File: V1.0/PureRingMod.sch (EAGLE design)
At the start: 32 parts, among them IC1 TL074P, IC2 TL072P, X1 NC3FD-V

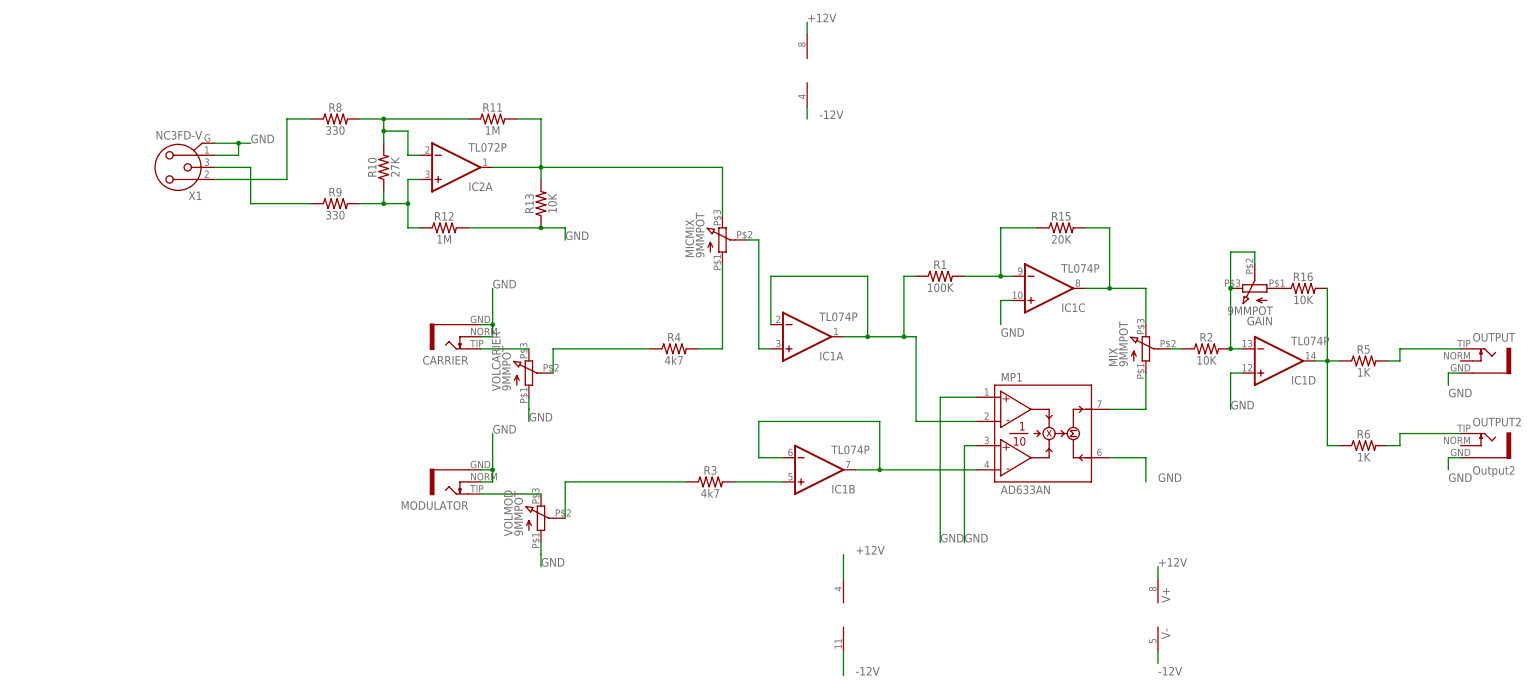
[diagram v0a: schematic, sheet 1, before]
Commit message: Panel layout and routing
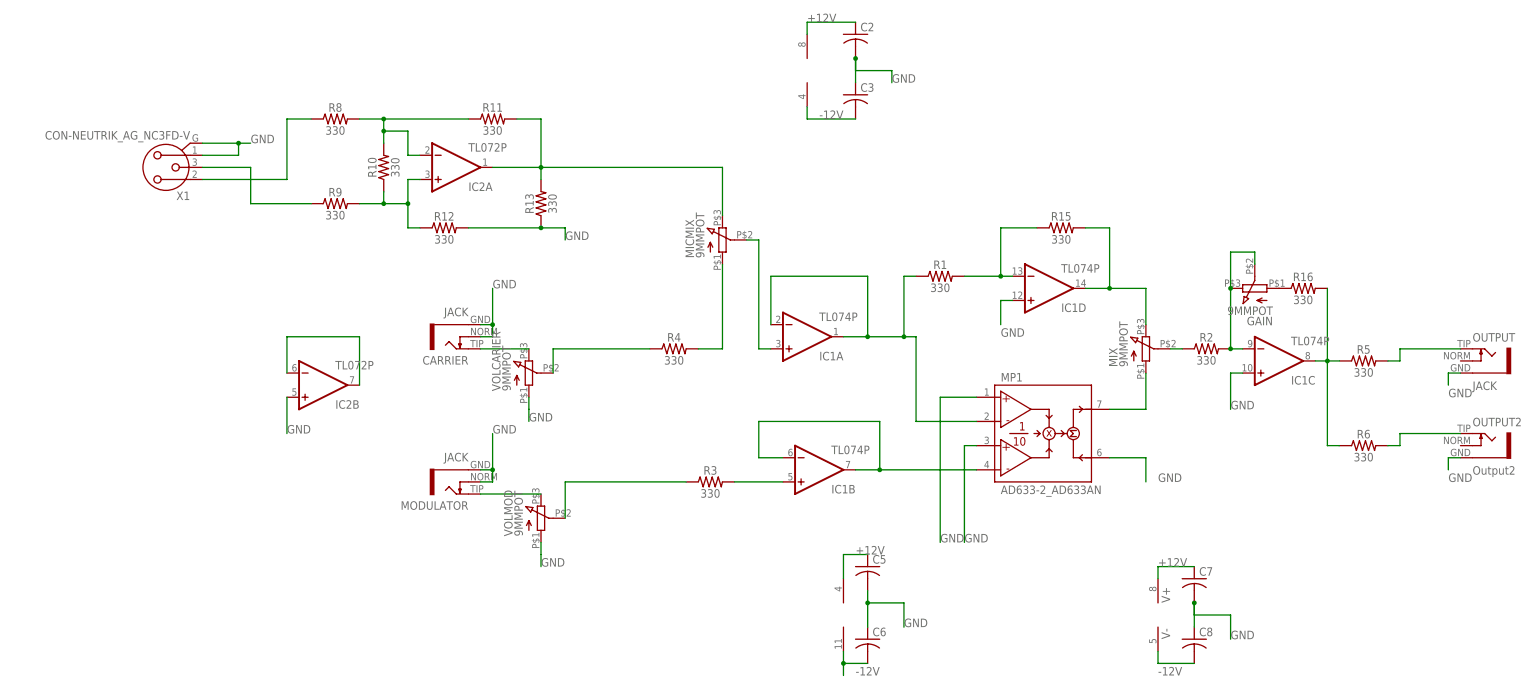
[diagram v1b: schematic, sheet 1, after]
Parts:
- added C2, C3, C5, C6, C7, C8: (no value), PureRingMod:CAPACITOR-US050-025X075
- C1, C4: device SparkFun-Capacitors:10UF-POLAR-RADIAL-2.5MM-25V-20% -> PureRingMod:10UF-POLAR-RADIAL-2.5MM-25V-20%
- CARRIER, MODULATOR, OUTPUT: value S_JACK -> JACK; device INSTRUO:S_JACK -> PureRingMod:JACK
- D1, D2: device adafruit:DIODEDO-1N4148 -> PureRingMod:DIODEDO-1N4148
- GAIN, MICMIX, MIX, VOLCARIER, VOLMOD: device GMSN:9MMPOT -> PureRingMod:9MMPOT
- IC1: device GMSN:TL074P -> PureRingMod:TL074P
- IC2: device GMSN-R2Project:TL072P -> PureRingMod:TL072P
- MP1: value AD633AN -> AD633-2_AD633AN; device ad633-2:AD633AN -> PureRingMod:AD633-2_AD633AN
- OUTPUT2: device INSTRUO:S_JACK -> PureRingMod:JACK
- POWER: device SparkFun-Connectors:M05X2SHD -> PureRingMod:M05X2SHD
- R1: value 100K -> 330; device SparkFun-Resistors:330OHM-HORIZ-1/10W-5% -> PureRingMod:330OHM-HORIZ-1/10W-5%
- R10: value 27K -> 330; device SparkFun-Resistors:330OHM-HORIZ-1/10W-5% -> PureRingMod:330OHM-HORIZ-1/10W-5%
- R11, R12: value 1M -> 330; device SparkFun-Resistors:330OHM-HORIZ-1/10W-5% -> PureRingMod:330OHM-HORIZ-1/10W-5%
- R13, R16, R2: value 10K -> 330; device SparkFun-Resistors:330OHM-HORIZ-1/10W-5% -> PureRingMod:330OHM-HORIZ-1/10W-5%
- R15: value 20K -> 330; device SparkFun-Resistors:330OHM-HORIZ-1/10W-5% -> PureRingMod:330OHM-HORIZ-1/10W-5%
- R3, R4: value 4k7 -> 330; device SparkFun-Resistors:330OHM-HORIZ-1/10W-5% -> PureRingMod:330OHM-HORIZ-1/10W-5%
- R5, R6: value 1K -> 330; device SparkFun-Resistors:330OHM-HORIZ-1/10W-5% -> PureRingMod:330OHM-HORIZ-1/10W-5%
- R8, R9: device SparkFun-Resistors:330OHM-HORIZ-1/10W-5% -> PureRingMod:330OHM-HORIZ-1/10W-5%
- X1: value NC3FD-V -> CON-NEUTRIK_AG_NC3FD-V; device con-neutrik_ag:NC3FD-V -> PureRingMod:CON-NEUTRIK_AG_NC3FD-V
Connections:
- new net N$13: IC2B.-IN, IC2B.OUT
- net +12V: now also C2.1, C5.1, C7.1
- net -12V: now also C3.2, C6.2, C8.2
- net GND: now also C2.2, C3.1, C5.2, C6.1, C7.2, C8.1, IC2B.+IN
- net N$12: now also IC1C.OUT; no longer IC1D.OUT
- net N$14: now also IC1D.-IN; no longer IC1C.-IN
- net N$4: now also IC1D.OUT; no longer IC1C.OUT
- net N$7: now also IC1C.-IN; no longer IC1D.-IN
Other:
- moved on the sheet: IC1C, IC1D, X1
